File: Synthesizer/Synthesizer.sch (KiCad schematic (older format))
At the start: 1 part

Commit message: Poorly laid out MIDI DAC subsystem
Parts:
- added GLIDE: R_POT, symbol Device:R_POT
- added R1: 5K, symbol Device:R
- added R2: 150, symbol Device:R
- added R3: 10k, symbol Device:R
- added U1: LM358, symbol Amplifier_Operational:LM358
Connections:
- net labels added: 5VOut, GND
- wire segments 0 -> 21
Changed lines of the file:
@@
 	1    0    0    -1
 $EndComp
+$Comp
+L Amplifier_Operational:LM358 U1
+U 1 1 5C54626A
+P 1050 6250
+F 0 "U1" H 1050 6617 50  0000 C CNN
+F 1 "LM358" H 1050 6526 50  0000 C CNN
+F 2 "" H 1050 6250 50  0001 C CNN
+F 3 "http://www.ti.com/lit/ds/symlink/lm2904-n.pdf" H 1050 6250 50  0001 C CNN
+	1    1050 6250
+	1    0    0    -1
+$EndComp
+$Comp
+L Device:R_POT GLIDE
+U 1 1 5C54647D
+P 1250 5600
+F 0 "GLIDE" H 1180 5646 50  0000 R CNN
+F 1 "R_POT" H 1180 5555 50  0000 R CNN
+F 2 "" H 1250 5600 50  0001 C CNN
+F 3 "~" H 1250 5600 50  0001 C CNN
+	1    1250 5600
+	-1   0    0    -1
+$EndComp
+Wire Wire Line
+	1100 5600 800  5600
+Wire Wire Line
+	800  5600 800  4450
+Wire Wire Line
+	800  4450 900  4450
+Wire Wire Line
+	2900 2050 3150 2050
+Wire Wire Line
+	3150 2050 3150 5350
+Wire Wire Line
+	3150 5350 1250 5350
+Wire Wire Line
+	1250 5350 1250 5450
+Wire Wire Line
+	900  950  750  950
+Wire Wire Line
+	750  950  750  600
+Wire Wire Line
+	750  600  3200 600
+Wire Wire Line
+	3200 600  3200 5750
+Wire Wire Line
+	3200 5750 1250 5750
+Wire Wire Line
+	900  4550 650  4550
+Wire Wire Line
+	650  4550 650  6150
+Wire Wire Line
+	650  6150 750  6150
+$Comp
+L Device:R R3
+U 1 1 5C546DCA
+P 750 6800
+F 0 "R3" H 820 6846 50  0000 L CNN
+F 1 "10k" H 820 6755 50  0000 L CNN
+F 2 "" V 680 6800 50  0001 C CNN
+F 3 "~" H 750 6800 50  0001 C CNN
+	1    750  6800
+	1    0    0    -1
+$EndComp
+Wire Wire Line
+	750  6650 750  6600
+Wire Wire Line
+	750  6600 950  6600
+Connection ~ 750  6600
+Wire Wire Line
+	750  6600 750  6350
+Text Label 1350 6250 0    50   ~ 0
+5VOut
+$Comp
+L power:GND #PWR?
+U 1 1 5C547323
+P 750 6950
+F 0 "#PWR?" H 750 6700 50  0001 C CNN
+F 1 "GND" H 755 6777 50  0000 C CNN
+F 2 "" H 750 6950 50  0001 C CNN
+F 3 "" H 750 6950 50  0001 C CNN
+	1    750  6950
+	1    0    0    -1
+$EndComp
+$Comp
+L Device:R R1
+U 1 1 5C5474EE
+P 1100 6600
+F 0 "R1" V 893 6600 50  0000 C CNN
+F 1 "5K" V 984 6600 50  0000 C CNN
+F 2 "" V 1030 6600 50  0001 C CNN
+F 3 "~" H 1100 6600 50  0001 C CNN
+	1    1100 6600
+	0    1    1    0
+$EndComp
+$Comp
+L Device:R R2
+U 1 1 5C547599
+P 1400 6600
+F 0 "R2" V 1607 6600 50  0000 C CNN
+F 1 "150" V 1516 6600 50  0000 C CNN
+F 2 "" V 1330 6600 50  0001 C CNN
+F 3 "~" H 1400 6600 50  0001 C CNN
+	1    1400 6600
+	0    -1   -1   0
+$EndComp
+Wire Wire Line
+	1550 6600 1650 6600
+Wire Wire Line
+	1650 6600 1650 6250
+Wire Wire Line
+	1650 6250 1350 6250
 $EndSCHEMATC

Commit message: Fuzz Face schematic added
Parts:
- added C1: 2.2uF, symbol Device:CP1
- added C2: 20uF, symbol Device:CP
- added C3: 0.01uF, symbol Device:C
- added FuzzInput, FuzzOutput: AudioJack2, symbol Connector:AudioJack2
- added GAIN: 1kB, symbol Device:R_POT
- added Q1, Q2: BC108, Package_TO_SOT_THT:TO-18-3, symbol Transistor_BJT:BC108
- added R1: 33k, symbol Device:R
- added R2: 100k, symbol Device:R
- added R3: 330, symbol Device:R
- added R4: 8k2, symbol Device:R
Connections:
- net labels added: +9V
- wire segments 21 -> 46

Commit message: Clean up DAC schematic
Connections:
- net labels added: 3.3V, GLIDE_IN, NOTE, NOTE_TO_VCO
- net labels removed: 5VOut
- wire segments 46 -> 41
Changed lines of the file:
@@
 EESchema Schematic File Version 4
+LIBS:Synthesizer-cache
 EELAYER 26 0
 EELAYER END
@@
 L Device:R_POT GLIDE
 U 1 1 5C54647D
-P 1250 5600
-F 0 "GLIDE" H 1180 5646 50  0000 R CNN
-F 1 "R_POT" H 1180 5555 50  0000 R CNN
-F 2 "" H 1250 5600 50  0001 C CNN
-F 3 "~" H 1250 5600 50  0001 C CNN
-	1    1250 5600
+P 1400 5600
+F 0 "GLIDE" H 1330 5646 50  0000 R CNN
+F 1 "R_POT" H 1330 5555 50  0000 R CNN
+F 2 "" H 1400 5600 50  0001 C CNN
+F 3 "~" H 1400 5600 50  0001 C CNN
+	1    1400 5600
 	-1   0    0    -1
 $EndComp
 Wire Wire Line
-	1100 5600 800  5600
-Wire Wire Line
-	800  5600 800  4450
-Wire Wire Line
-	800  4450 900  4450
-Wire Wire Line
-	2900 2050 3150 2050
-Wire Wire Line
-	3150 2050 3150 5350
-Wire Wire Line
-	3150 5350 1250 5350
-Wire Wire Line
-	1250 5350 1250 5450
-Wire Wire Line
 	900  950  750  950
 Wire Wire Line
@@
 Wire Wire Line
 	750  600  3200 600
-Wire Wire Line
-	3200 600  3200 5750
-Wire Wire Line
-	3200 5750 1250 5750
-Wire Wire Line
-	900  4550 650  4550
-Wire Wire Line
-	650  4550 650  6150
-Wire Wire Line
-	650  6150 750  6150
 $Comp
 L Device:R R3
@@
 Wire Wire Line
 	750  6600 750  6350
-Text Label 1350 6250 0    50   ~ 0
-5VOut
 $Comp
 L power:GND #PWR?
@@
 	7850 750  7850 800
 Connection ~ 7850 800
+Text Label 550  4450 0    50   ~ 0
+GLIDE_IN
+Text Label 700  4550 0    50   ~ 0
+NOTE
+Wire Wire Line
+	900  4550 700  4550
+Wire Wire Line
+	900  4450 550  4450
+Text Label 1400 5400 0    50   ~ 0
+3.3V
+Wire Wire Line
+	1400 5450 1400 5400
+$Comp
+L power:GND #PWR?
+U 1 1 5C5B4A50
+P 1400 5850
+F 0 "#PWR?" H 1400 5600 50  0001 C CNN
+F 1 "GND" H 1405 5677 50  0000 C CNN
+F 2 "" H 1400 5850 50  0001 C CNN
+F 3 "" H 1400 5850 50  0001 C CNN
+	1    1400 5850
+	1    0    0    -1
+$EndComp
+Wire Wire Line
+	1400 5750 1400 5850
+Text Label 850  5600 0    50   ~ 0
+GLIDE_IN
+Wire Wire Line
+	850  5600 1250 5600
+Text Label 550  6150 0    50   ~ 0
+NOTE
+Wire Wire Line
+	550  6150 750  6150
+Text Label 1800 6250 0    50   ~ 0
+NOTE_TO_VCO
+Wire Wire Line
+	1800 6250 1650 6250
+Connection ~ 1650 6250
 $EndSCHEMATC

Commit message: Create rats nest for pcb layout
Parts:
- removed FuzzInput, FuzzOutput: AudioJack2, symbol Connector:AudioJack2
- removed GAIN: 1kB, symbol Device:R_POT
- removed GLIDE: R_POT, symbol Device:R_POT
- added FUZZ_GAIN1, GLIDE_POT1: Conn_01x03_Male, Connector_Wire:SolderWirePad_1x03_P4.445mm_Drill1.5mm, symbol Connector:Conn_01x03_Male
- added FUZZ_IN1, FUZZ_OUT1: Conn_01x02_Male, Connector_Wire:SolderWirePad_1x02_P5.08mm_Drill1.5mm, symbol Connector:Conn_01x02_Male
- C1: footprint (none) -> Capacitor_THT:CP_Radial_D10.0mm_P5.00mm
- C2: renamed from C3; footprint (none) -> Capacitor_THT:C_Disc_D6.0mm_W2.5mm_P5.00mm
- C3: renamed from C2; footprint (none) -> Capacitor_THT:CP_Radial_D10.0mm_P5.00mm
- R1, R5: renamed from R3; footprint (none) -> Resistor_THT:R_Axial_DIN0207_L6.3mm_D2.5mm_P10.16mm_Horizontal
- R2, R4: renamed from R1; footprint (none) -> Resistor_THT:R_Axial_DIN0207_L6.3mm_D2.5mm_P10.16mm_Horizontal
- R3, R6: renamed from R2; footprint (none) -> Resistor_THT:R_Axial_DIN0207_L6.3mm_D2.5mm_P10.16mm_Horizontal
- R7: renamed from R4; footprint (none) -> Resistor_THT:R_Axial_DIN0207_L6.3mm_D2.5mm_P10.16mm_Horizontal
- U1: footprint (none) -> Package_DIP:DIP-8_W7.62mm_Socket
- U2: renamed from U?; footprint (none) -> Teensy:Teensy35_36
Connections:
- wire segments 41 -> 46

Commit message: Add buffer for fuzz
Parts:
- added U3: TL071, Package_DIP:DIP-8_W7.62mm_Socket, symbol Amplifier_Operational:TL071
- U2: symbol teensy:Teensy3.6 -> Synthesizer-rescue:Teensy3.6-teensy
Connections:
- net +9V: now also U3.7 (V+)
- net GND: now also U3.4 (V-)
- net at C1.2: now also U3.2 (-), U3.6; no longer FUZZ_IN1.2 (Pin_2)
- new net: FUZZ_IN1.2 (Pin_2), U3.3 (+)
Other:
- moved on the sheet: FUZZ_IN1
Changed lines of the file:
@@
 $EndDescr
 $Comp
-L teensy:Teensy3.6 U2
+L Synthesizer-rescue:Teensy3.6-teensy U2
 U 1 1 5C545E1F
 P 1900 3050
@@
 	9300 800  8900 800
 Wire Wire Line
-	7100 750  7850 750
+	7100 750  7250 750
 Wire Wire Line
 	7850 750  7850 800
@@
 L Connector:Conn_01x02_Male FUZZ_IN1
 U 1 1 5C6DAD71
-P 6750 1250
-F 0 "FUZZ_IN1" H 6856 1428 50  0000 C CNN
-F 1 "Conn_01x02_Male" H 6856 1337 50  0000 C CNN
-F 2 "Connector_Wire:SolderWirePad_1x02_P5.08mm_Drill1.5mm" H 6750 1250 50  0001 C CNN
-F 3 "~" H 6750 1250 50  0001 C CNN
-	1    6750 1250
-	1    0    0    -1
-$EndComp
-Wire Wire Line
-	6950 1350 7150 1350
+P 6100 1250
+F 0 "FUZZ_IN1" H 6206 1428 50  0000 C CNN
+F 1 "Conn_01x02_Male" H 6206 1337 50  0000 C CNN
+F 2 "Connector_Wire:SolderWirePad_1x02_P5.08mm_Drill1.5mm" H 6100 1250 50  0001 C CNN
+F 3 "~" H 6100 1250 50  0001 C CNN
+	1    6100 1250
+	1    0    0    -1
+$EndComp
 $Comp
 L power:GND #PWR0102
 U 1 1 5C6DD678
-P 7000 1550
-F 0 "#PWR0102" H 7000 1300 50  0001 C CNN
-F 1 "GND" H 7005 1377 50  0000 C CNN
-F 2 "" H 7000 1550 50  0001 C CNN
-F 3 "" H 7000 1550 50  0001 C CNN
-	1    7000 1550
-	1    0    0    -1
-$EndComp
-Wire Wire Line
-	7000 1550 7000 1250
-Wire Wire Line
-	7000 1250 6950 1250
+P 6400 1550
+F 0 "#PWR0102" H 6400 1300 50  0001 C CNN
+F 1 "GND" H 6405 1377 50  0000 C CNN
+F 2 "" H 6400 1550 50  0001 C CNN
+F 3 "" H 6400 1550 50  0001 C CNN
+	1    6400 1550
+	1    0    0    -1
+$EndComp
 $Comp
 L Connector:Conn_01x02_Male FUZZ_OUT1
@@
 Wire Wire Line
 	850  5600 1400 5600
+$Comp
+L Amplifier_Operational:TL071 U3
+U 1 1 5C8282EB
+P 6800 1350
+F 0 "U3" H 7141 1396 50  0000 L CNN
+F 1 "TL071" H 7141 1305 50  0000 L CNN
+F 2 "Package_DIP:DIP-8_W7.62mm_Socket" H 6850 1400 50  0001 C CNN
+F 3 "http://www.ti.com/lit/ds/symlink/tl071.pdf" H 6950 1500 50  0001 C CNN
+	1    6800 1350
+	1    0    0    -1
+$EndComp
+Wire Wire Line
+	6400 1550 6400 1250
+Wire Wire Line
+	6400 1250 6300 1250
+Wire Wire Line
+	6300 1350 6500 1350
+Wire Wire Line
+	6500 1350 6500 1250
+Wire Wire Line
+	7100 1350 7150 1350
+Wire Wire Line
+	7100 1350 7100 1800
+Wire Wire Line
+	7100 1800 6500 1800
+Wire Wire Line
+	6500 1800 6500 1450
+Connection ~ 7100 1350
+$Comp
+L power:GND #PWR0103
+U 1 1 5C82AD33
+P 6700 1850
+F 0 "#PWR0103" H 6700 1600 50  0001 C CNN
+F 1 "GND" H 6705 1677 50  0000 C CNN
+F 2 "" H 6700 1850 50  0001 C CNN
+F 3 "" H 6700 1850 50  0001 C CNN
+	1    6700 1850
+	1    0    0    -1
+$EndComp
+Wire Wire Line
+	6700 1850 6700 1650
+Wire Wire Line
+	6700 1050 7250 1050
+Wire Wire Line
+	7250 1050 7250 750
+Connection ~ 7250 750
+Wire Wire Line
+	7250 750  7850 750
 $EndSCHEMATC

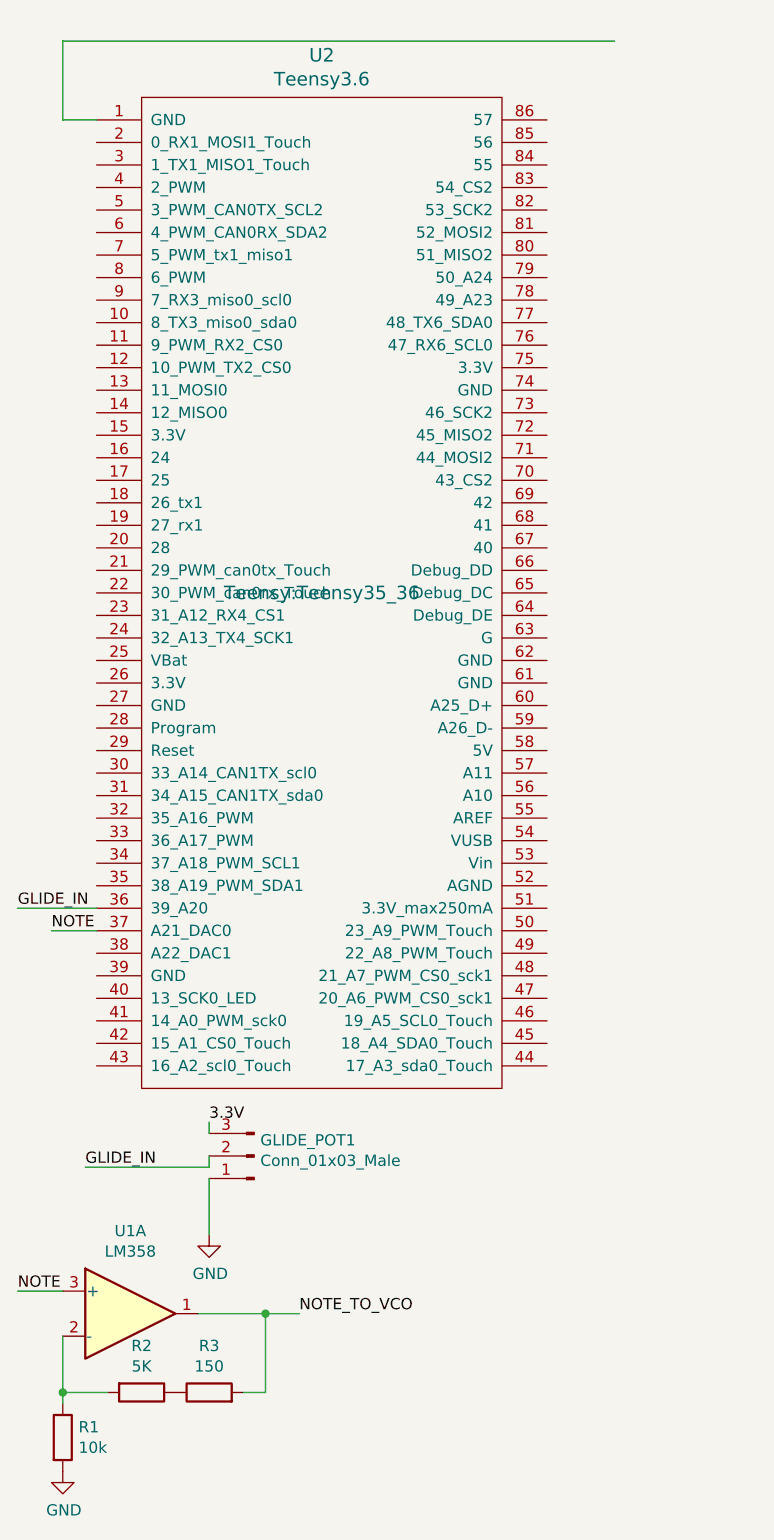
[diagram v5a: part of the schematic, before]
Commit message: Remove DAC circuit
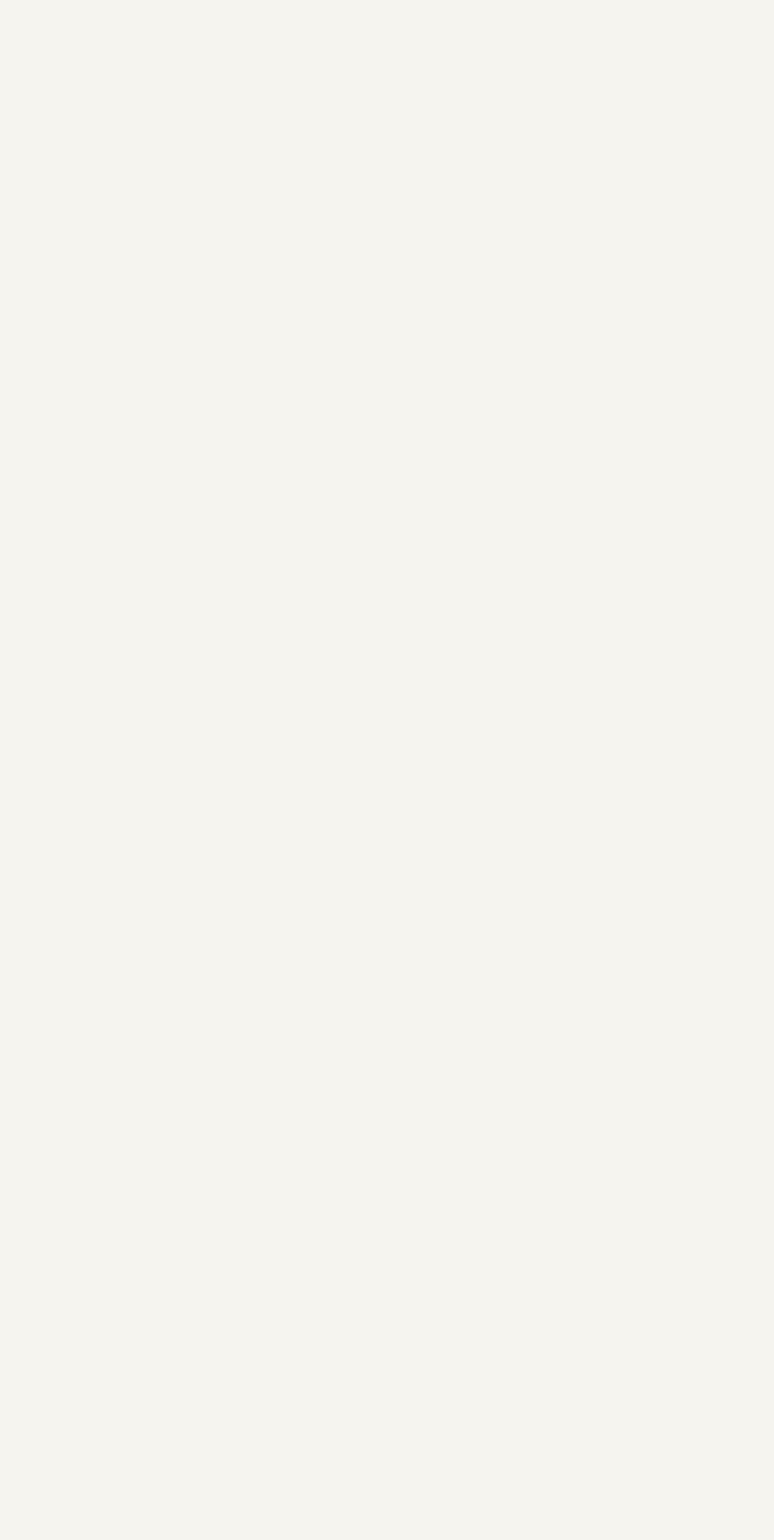
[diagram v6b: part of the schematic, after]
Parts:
- removed GLIDE_POT1: Conn_01x03_Male, Connector_Wire:SolderWirePad_1x03_P4.445mm_Drill1.5mm, symbol Connector:Conn_01x03_Male
- removed R1: 10k, Resistor_THT:R_Axial_DIN0207_L6.3mm_D2.5mm_P10.16mm_Horizontal, symbol Device:R
- removed R2: 5K, Resistor_THT:R_Axial_DIN0207_L6.3mm_D2.5mm_P10.16mm_Horizontal, symbol Device:R
- removed R3: 150, Resistor_THT:R_Axial_DIN0207_L6.3mm_D2.5mm_P10.16mm_Horizontal, symbol Device:R
- removed U1: LM358, Package_DIP:DIP-8_W7.62mm_Socket, symbol Amplifier_Operational:LM358
- removed U2: Teensy3.6, Teensy:Teensy35_36, symbol Synthesizer-rescue:Teensy3.6-teensy
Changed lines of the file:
@@
 $EndDescr
-$Comp
-L Synthesizer-rescue:Teensy3.6-teensy U2
-U 1 1 5C545E1F
-P 1900 3050
-F 0 "U2" H 1900 5437 60  0000 C CNN
-F 1 "Teensy3.6" H 1900 5331 60  0000 C CNN
-F 2 "Teensy:Teensy35_36" H 1900 3050 60  0000 C CNN
-F 3 "" H 1900 3050 60  0000 C CNN
-	1    1900 3050
-	1    0    0    -1
-$EndComp
-$Comp
-L Amplifier_Operational:LM358 U1
-U 1 1 5C54626A
-P 1050 6250
-F 0 "U1" H 1050 6617 50  0000 C CNN
-F 1 "LM358" H 1050 6526 50  0000 C CNN
-F 2 "Package_DIP:DIP-8_W7.62mm_Socket" H 1050 6250 50  0001 C CNN
-F 3 "http://www.ti.com/lit/ds/symlink/lm2904-n.pdf" H 1050 6250 50  0001 C CNN
-	1    1050 6250
-	1    0    0    -1
-$EndComp
-Wire Wire Line
-	900  950  750  950
-Wire Wire Line
-	750  950  750  600
-Wire Wire Line
-	750  600  3200 600
-$Comp
-L Device:R R1
-U 1 1 5C546DCA
-P 750 6800
-F 0 "R1" H 820 6846 50  0000 L CNN
-F 1 "10k" H 820 6755 50  0000 L CNN
-F 2 "Resistor_THT:R_Axial_DIN0207_L6.3mm_D2.5mm_P10.16mm_Horizontal" V 680 6800 50  0001 C CNN
-F 3 "~" H 750 6800 50  0001 C CNN
-	1    750  6800
-	1    0    0    -1
-$EndComp
-Wire Wire Line
-	750  6650 750  6600
-Wire Wire Line
-	750  6600 950  6600
-Connection ~ 750  6600
-Wire Wire Line
-	750  6600 750  6350
-$Comp
-L power:GND #PWR01
-U 1 1 5C547323
-P 750 6950
-F 0 "#PWR01" H 750 6700 50  0001 C CNN
-F 1 "GND" H 755 6777 50  0000 C CNN
-F 2 "" H 750 6950 50  0001 C CNN
-F 3 "" H 750 6950 50  0001 C CNN
-	1    750  6950
-	1    0    0    -1
-$EndComp
-$Comp
-L Device:R R2
-U 1 1 5C5474EE
-P 1100 6600
-F 0 "R2" V 893 6600 50  0000 C CNN
-F 1 "5K" V 984 6600 50  0000 C CNN
-F 2 "Resistor_THT:R_Axial_DIN0207_L6.3mm_D2.5mm_P10.16mm_Horizontal" V 1030 6600 50  0001 C CNN
-F 3 "~" H 1100 6600 50  0001 C CNN
-	1    1100 6600
-	0    1    1    0
-$EndComp
-$Comp
-L Device:R R3
-U 1 1 5C547599
-P 1400 6600
-F 0 "R3" V 1607 6600 50  0000 C CNN
-F 1 "150" V 1516 6600 50  0000 C CNN
-F 2 "Resistor_THT:R_Axial_DIN0207_L6.3mm_D2.5mm_P10.16mm_Horizontal" V 1330 6600 50  0001 C CNN
-F 3 "~" H 1400 6600 50  0001 C CNN
-	1    1400 6600
-	0    -1   -1   0
-$EndComp
-Wire Wire Line
-	1550 6600 1650 6600
-Wire Wire Line
-	1650 6600 1650 6250
-Wire Wire Line
-	1650 6250 1350 6250
 $Comp
 L Transistor_BJT:BC108 Q1
@@
 	7850 750  7850 800
 Connection ~ 7850 800
-Text Label 550  4450 0    50   ~ 0
-GLIDE_IN
-Text Label 700  4550 0    50   ~ 0
-NOTE
-Wire Wire Line
-	900  4550 700  4550
-Wire Wire Line
-	900  4450 550  4450
-Text Label 1400 5400 0    50   ~ 0
-3.3V
-Wire Wire Line
-	1400 5450 1400 5400
-Text Label 850  5600 0    50   ~ 0
-GLIDE_IN
-Text Label 550  6150 0    50   ~ 0
-NOTE
-Wire Wire Line
-	550  6150 750  6150
-Text Label 1800 6250 0    50   ~ 0
-NOTE_TO_VCO
-Wire Wire Line
-	1800 6250 1650 6250
-Connection ~ 1650 6250
 $Comp
 L power:GND #PWR05
@@
 	7550 1800 8050 1800
 Connection ~ 7550 1350
-$Comp
-L power:GND #PWR0101
-U 1 1 5C6D8A0E
-P 1400 5900
-F 0 "#PWR0101" H 1400 5650 50  0001 C CNN
-F 1 "GND" H 1405 5727 50  0000 C CNN
-F 2 "" H 1400 5900 50  0001 C CNN
-F 3 "" H 1400 5900 50  0001 C CNN
-	1    1400 5900
-	1    0    0    -1
-$EndComp
 $Comp
 L Connector:Conn_01x02_Male FUZZ_IN1
@@
 	8750 2200 8750 2050
 $Comp
-L Connector:Conn_01x03_Male GLIDE_POT1
-U 1 1 5C6E177E
-P 1600 5550
-F 0 "GLIDE_POT1" H 1573 5480 50  0000 R CNN
-F 1 "Conn_01x03_Male" H 1573 5571 50  0000 R CNN
-F 2 "Connector_Wire:SolderWirePad_1x03_P4.445mm_Drill1.5mm" H 1600 5550 50  0001 C CNN
-F 3 "~" H 1600 5550 50  0001 C CNN
-	1    1600 5550
-	-1   0    0    1
-$EndComp
-Wire Wire Line
-	1400 5650 1400 5900
-Wire Wire Line
-	1400 5550 1400 5600
-Wire Wire Line
-	850  5600 1400 5600
-$Comp
 L Amplifier_Operational:TL071 U3
